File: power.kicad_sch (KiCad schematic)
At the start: 6 parts, among them U6 REF3030, U7 MIC920YC5-TR

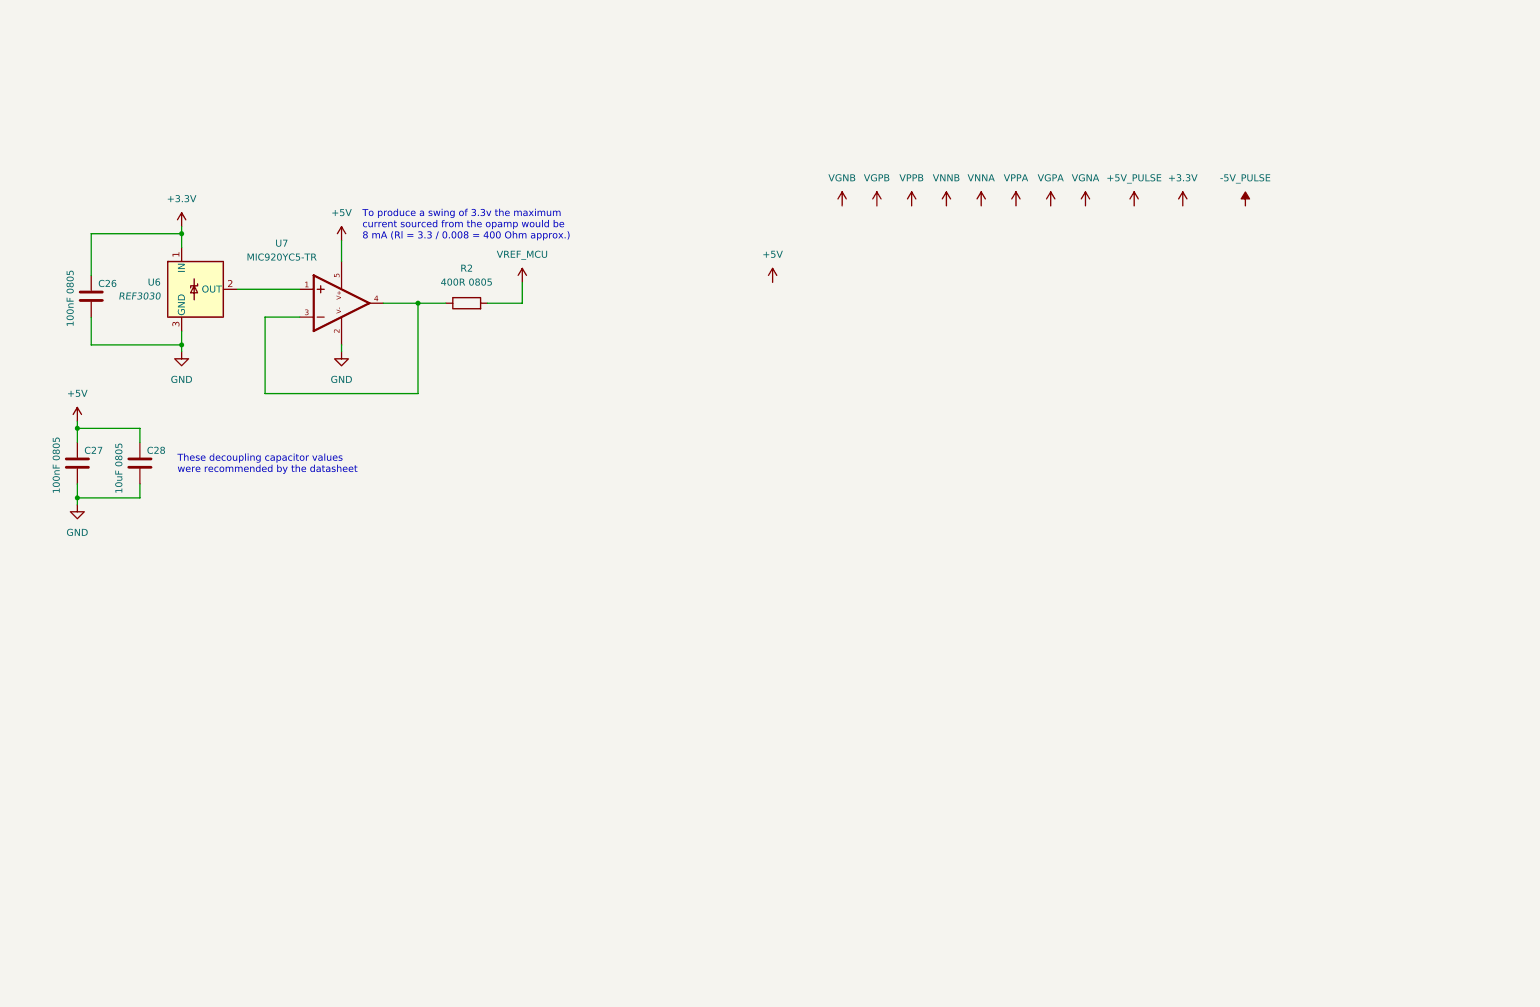
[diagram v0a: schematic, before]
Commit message: finished analog signal chain, added main power components, complete the schematic and form a power budget table
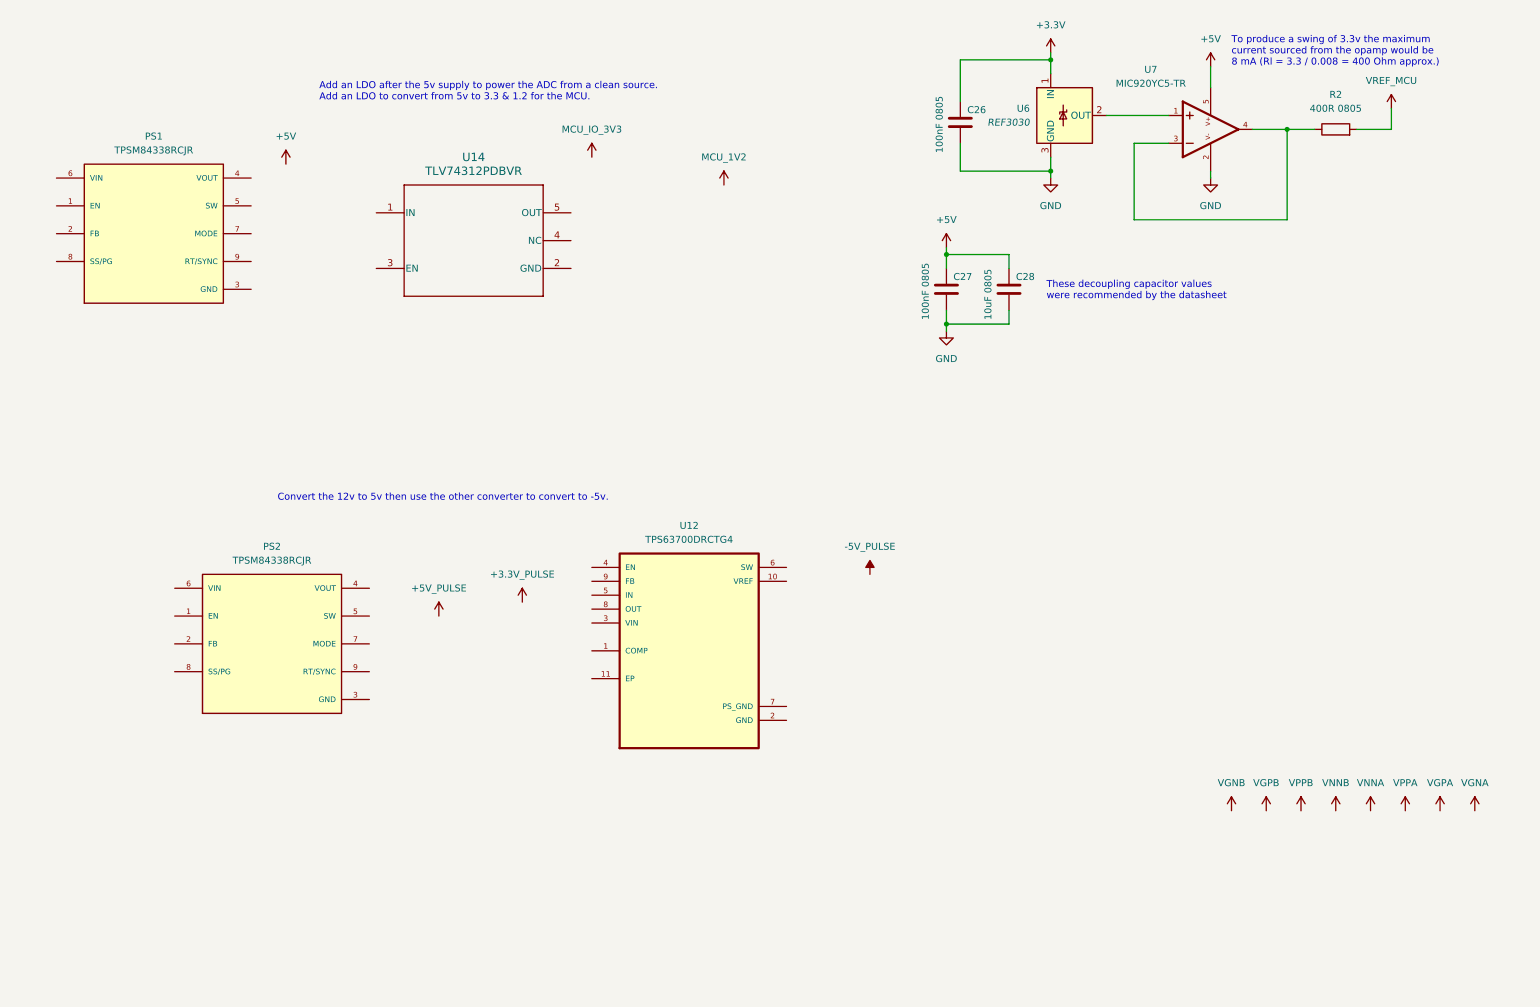
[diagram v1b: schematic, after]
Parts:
- added PS1, PS2: TPSM84338RCJR, TPSM84338RCJR:CONV_TPSM84338RCJR, symbol TPSM84338RCJR:TPSM84338RCJR
- added U12: TPS63700DRCTG4, TPS63700DRCTG4:VREG_V62_16624-01YE, symbol TPS63700DRCTG4:TPS63700DRCTG4
- added U14: TLV74312PDBVR, DBV0005A_N, symbol TLV74312PDBVR:TLV74312PDBVR
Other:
- note added: "Add an LDO after the 5v supply to power the ADC from a clean source. Add an LDO to convert from 5v to 3.3 & 1.2 for the MCU."
- note added: "Convert the 12v to 5v then use the other converter to convert to -5v."
- moved on the sheet: C26, C27, C28, R2, U6, U7

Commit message: finished 50% of power section, 50% remaining + EEPROM & revision
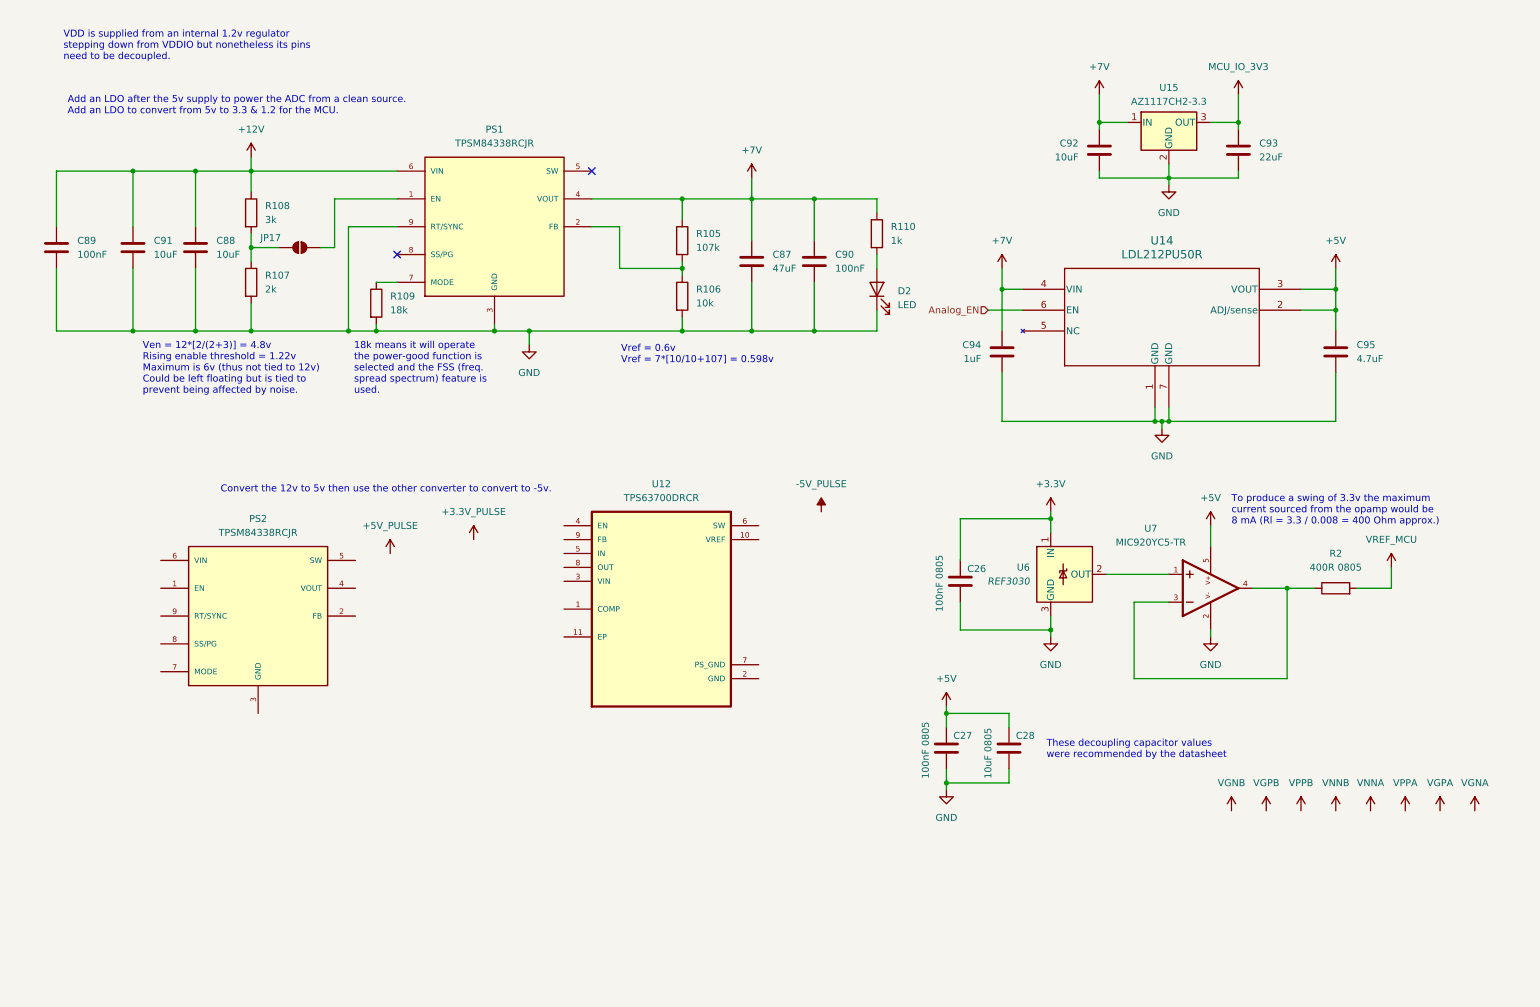
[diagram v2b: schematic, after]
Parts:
- removed U12: TPS63700DRCTG4, TPS63700DRCTG4:VREG_V62_16624-01YE, symbol TPS63700DRCTG4:TPS63700DRCTG4
- removed U14: TLV74312PDBVR, DBV0005A_N, symbol TLV74312PDBVR:TLV74312PDBVR
- added C87: 47uF, symbol Device:C
- added C88, C91, C92: 10uF, symbol Device:C
- added C89, C90: 100nF, symbol Device:C
- added C93: 22uF, symbol Device:C
- added C94: 1uF, symbol Device:C
- added C95: 4.7uF, symbol Device:C
- added D2: LED, symbol Device:LED
- added JP17: SolderJumper_2_Open, symbol Jumper:SolderJumper_2_Open
- added R105: 107k, symbol Device:R
- added R106: 10k, symbol Device:R
- added R107: 2k, symbol Device:R
- added R108: 3k, symbol Device:R
- added R109: 18k, symbol Device:R
- added R110: 1k, symbol Device:R
- added U12: TPS63700DRCR, TPS63700DRCR:VREG_V62_16624-01YE, symbol TPS63700DRCR:TPS63700DRCR
- added U14: LDL212PU50R, DFN_2PU50R_STM, symbol 2025-12-15_21-20-32:LDL212PU50R
- added U15: AZ1117CH2-3.3, Package_TO_SOT_SMD:SOT-223-3_TabPin2, symbol Regulator_Linear:AZ1117CH2-3.3
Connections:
- net +5V: now also C95.1, U14.2 (ADJ/sense), U14.3 (VOUT)
- net GND: now also PS1.3 (GND), PS1.9 (RT/SYNC), C87.2, C88.2, C89.2, C90.2, C91.2, C92.2, C93.2, C94.2, C95.2, D2.1 (K), R106.2, R107.2, R109.2, U14.1 (GND), U14.7 (GND), U15.2 (GND)
- net MCU_IO_3V3: now also C93.1, U15.3 (OUT)
- net at PS1.1 (EN): now also JP17.2 (B)
- net at PS1.2 (FB): now also R105.2, R106.1
- net +7V: now reaches PS1.4 (VOUT)
- net +7V: now also C87.1, C90.1, C92.1, C94.1, R105.1, R110.1, U14.4 (VIN), U15.1 (IN)
- net +12V: now reaches PS1.6 (VIN)
- net +12V: now also C88.1, C89.1, C91.1, R108.1
- net at PS1.7 (MODE): now also R109.1
- new net: JP17.1 (A), R107.1, R108.2
- new net: D2.2 (A), R110.2
- new net Analog_EN: U14.6 (EN)
- no-connect marks 0 -> 2
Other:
- note added: "18k means it will operate the power-good function is selected and the FSS (freq. spread spectrum) feature is used."
- note added: "VDD is supplied from an internal 1.2v regulator stepping down from VDDIO but nonetheless its pins need to be decoupled."
- note added: "Ven = 12*[2/(2+3)] = 4.8v Rising enable threshold = 1.22v Maximum is 6v (thus not tied to 12v) Could be left floating but is tied to prevent being affected by noise."
- note added: "Vref = 0.6v Vref = 7*[10/10+107] = 0.598v"
- moved on the sheet: C26, C27, C28, PS1, R2, U6, U7

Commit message: 95% done, only headers for communication & power are remaining + RS232 transceiver & 1.5v reference
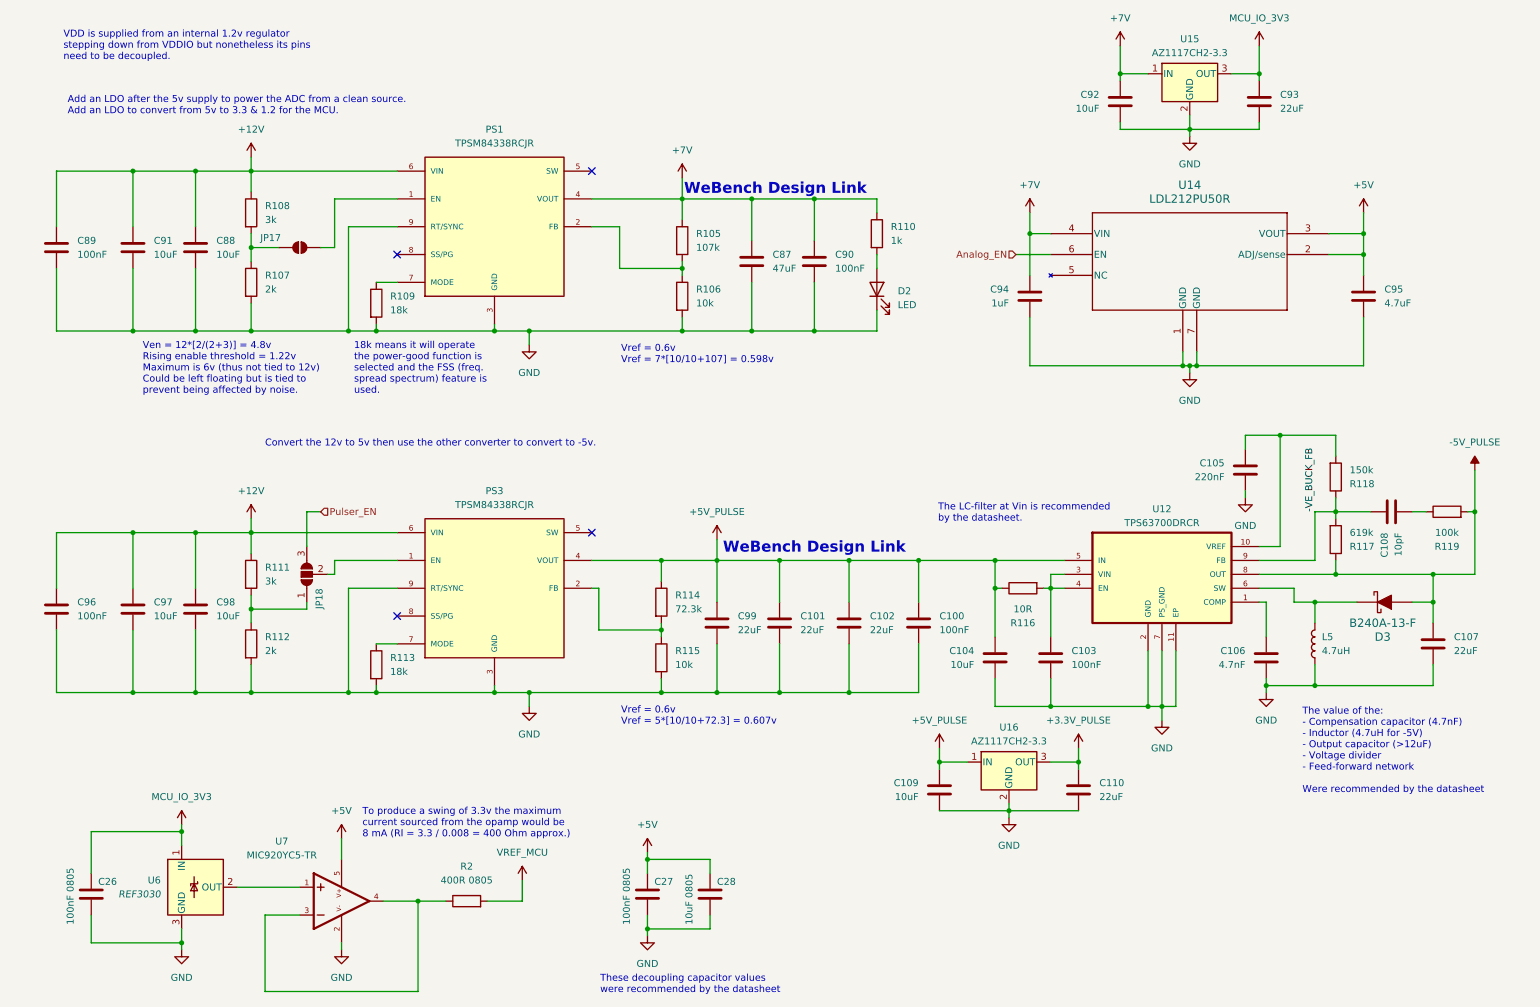
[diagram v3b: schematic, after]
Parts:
- removed PS2: TPSM84338RCJR, TPSM84338RCJR:CONV_TPSM84338RCJR, symbol TPSM84338RCJR:TPSM84338RCJR
- added C100, C103, C96: 100nF, symbol Device:C
- added C101, C102, C107, C110, C99: 22uF, symbol Device:C
- added C104, C109, C97, C98: 10uF, symbol Device:C
- added C105: 220nF, symbol Device:C
- added C106: 4.7nF, symbol Device:C
- added C108: 10pF, symbol Device:C
- added D3: B240A-13-F, digikey-footprints:DO-214AC, symbol dk_Diodes-Rectifiers-Single:B240A-13-F
- added JP18: SolderJumper_3_Open, symbol Jumper:SolderJumper_3_Open
- added L5: 4.7uH, symbol Device:L
- added PS3: TPSM84338RCJR, TPSM84338RCJR:CONV_TPSM84338RCJR, symbol TPSM84338RCJR:TPSM84338RCJR
- added R111: 3k, symbol Device:R
- added R112: 2k, symbol Device:R
- added R113: 18k, symbol Device:R
- added R114: 72.3k, symbol Device:R
- added R115: 10k, symbol Device:R
- added R116: 10R, symbol Device:R
- added R117: 619k, symbol Device:R
- added R118: 150k, symbol Device:R
- added R119: 100k, symbol Device:R
- added U16: AZ1117CH2-3.3, Package_TO_SOT_SMD:SOT-223-3_TabPin2, symbol Regulator_Linear:AZ1117CH2-3.3
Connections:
- net +3.3V is gone; now on net MCU_IO_3V3: C26.1, U6.1 (IN)
- net +12V: now also C96.1, C97.1, C98.1, PS3.6 (VIN), R111.1
- net +3.3V_PULSE: now also C110.1, U16.3 (OUT)
- net +5V_PULSE: now also U12.5 (IN), C100.1, C101.1, C102.1, C104.1, C109.1, C99.1, PS3.4 (VOUT), R114.1, R116.1, U16.1 (IN)
- net -5V_PULSE: now also U12.8 (OUT), C107.1, D3.A, R117.1, R119.2
- net GND: now also U12.11 (EP), U12.2 (GND), U12.7 (PS_GND), C100.2, C101.2, C102.2, C103.2, C104.2, C105.2, C106.2, C107.2, C109.2, C110.2, C96.2, C97.2, C98.2, C99.2, L5.1, PS3.3 (GND), PS3.9 (RT/SYNC), R112.2, R113.2, R115.2, U16.2 (GND)
- net at U12.1 (COMP): now also C106.1
- net at U12.10 (VREF): now also C105.1, R118.2
- net at U12.3 (VIN): now also U12.4 (EN), C103.1, R116.2
- net at U12.6 (SW): now also D3.K, L5.2
- net -VE_BUCK_FB: now reaches U12.9 (FB)
- net -VE_BUCK_FB: now also C108.1, R117.2, R118.1
- new net: JP18.1 (A), R111.2, R112.1
- new net: PS3.2 (FB), R114.2, R115.1
- new net: JP18.2 (C), PS3.1 (EN)
- new net: PS3.7 (MODE), R113.1
- new net: C108.2, R119.1
- new net Pulser_EN: JP18.3 (B)
- no-connect marks 2 -> 4
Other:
- note added: "The LC-filter at Vin is recommended by the datasheet."
- note added: "The value of the: - Compensation capacitor (4.7nF) - Inductor (4.7uH for -5V) - Output capacitor (>12uF) - Voltage divider - Feed-forward network Were recommended by the datasheet"
- note added: "Vref = 0.6v Vref = 5*[10/10+72.3] = 0.607v"
- note added: "WeBench Design Link"
- moved on the sheet: C26, C27, C28, C92, C93, C94, C95, R2, U12, U14, U15, U6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

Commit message: DONE (inshallah)
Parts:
- added D4, D5, D6, D7, D8: LED, symbol Device:LED
- added J17: Input Power, symbol Connector:Screw_Terminal_01x02
- added R136, R137: 1k, symbol Device:R
- added R138: 2k, symbol Device:R
- added R139, R140: 330R, symbol Device:R
- added TP73, TP74, TP75, TP76, TP77, TP78, TP79, TP80, TP81: RCT-0C, digikey-footprints:PROBE_PAD_0805, symbol dk_Test-Points:RCT-0C
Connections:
- net +12V: now also J17.1 (Pin_1), R138.1, TP73.1
- net +3.3V_PULSE: now also R140.1, TP78.1
- net +5V: now also R137.1, TP77.1
- net +5V_PULSE: now also R136.1, TP75.1
- net +7V: now also TP74.1
- net -5V_PULSE: now also TP76.1
- net GND: now also D4.1 (K), D5.1 (K), D6.1 (K), D7.1 (K), D8.1 (K), J17.2 (Pin_2)
- net MCU_IO_3V3: now also R139.1, TP79.1
- net VREF_MCU: now also TP80.1
- net at U6.2 (OUT), U7.1: now also TP81.1
- new net: D6.2 (A), R138.2
- new net: D8.2 (A), R140.2
- new net: D7.2 (A), R139.2
- new net: D4.2 (A), R136.2
- new net: D5.2 (A), R137.2
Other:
- note added: "The values of the: - Compensation capacitor (4.7nF) - Inductor (4.7uH for -5V) - Output capacitor (>12uF) - Voltage divider - Feed-forward network Were recommended by the datasheet"
- note removed: "Add an LDO after the 5v supply to power the ADC from a clean source. Add an LDO to convert from 5v to 3.3 & 1.2 for the MCU."
- note removed: "The value of the: - Compensation capacitor (4.7nF) - Inductor (4.7uH for -5V) - Output capacitor (>12uF) - Voltage divider - Feed-forward network Were recommended by the datasheet"

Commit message: started layout, 20-30% done
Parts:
- added J26: Spectrography Power, Connector_PinHeader_2.54mm:PinHeader_1x02_P2.54mm_Vertical, symbol Connector:Conn_01x02_Pin
- C100, C103, C105, C106, C108, C26, C27, C28, C89, C90, C94, C96: footprint (none) -> Capacitor_SMD:C_0603_1608Metric
- C101, C102, C104, C107, C109, C110, C88, C91, C92, C93, C95, C97, C98, C99: footprint (none) -> Capacitor_SMD:C_0805_2012Metric
- C87: footprint (none) -> Capacitor_SMD:C_1210_3225Metric
- D2, D4, D5, D6, D7, D8: footprint (none) -> LED_SMD:LED_0805_2012Metric
- J17: footprint (none) -> TerminalBlock:TerminalBlock_MaiXu_MX126-5.0-02P_1x02_P5.00mm
- JP17: footprint (none) -> Jumper:SolderJumper-2_P1.3mm_Open_Pad1.0x1.5mm
- JP18: footprint (none) -> Jumper:SolderJumper-3_P1.3mm_Open_Pad1.0x1.5mm
- L5: footprint (none) -> Inductor_SMD:L_0805_2012Metric
- R105, R106, R107, R108, R109, R110, R111, R112, R113, R114, R115, R116, R117, R118, R119, R136, R137, R138, R139, R140, R2: footprint (none) -> Resistor_SMD:R_0603_1608Metric
- U14: footprint DFN_2PU50R_STM -> LDL212PU50R:DFN_2PU50R_STM
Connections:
- net +12V: now also J26.1 (Pin_1)
- net GND: now also J26.2 (Pin_2)
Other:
- note removed: "Convert the 12v to 5v then use the other converter to convert to -5v."

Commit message: 5% left, rearrange ADC channels for right AFE
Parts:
- added JP10, JP13, JP6, JP8, JP9: SolderJumper_2_Open, Jumper:SolderJumper-2_P1.3mm_Open_RoundedPad1.0x1.5mm, symbol Jumper:SolderJumper_2_Open
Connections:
- net +12V: now also JP6.1 (A), JP8.1 (A); no longer C88.1, C89.1, C91.1, C96.1, C97.1, C98.1, PS1.6 (VIN), PS3.6 (VIN), R108.1, R111.1, TP73.1
- net +5V: now also JP13.1 (A); no longer C27.1, C28.1, U7.5
- net +7V: now also JP9.1 (A); no longer C92.1, C94.1, U14.4 (VIN), U15.1 (IN)
- net MCU_IO_3V3: now also JP10.2 (B); no longer C93.1, R139.1, TP79.1, U15.3 (OUT)
- new net +12V_VFD: C88.1, C89.1, C91.1, C96.1, C97.1, C98.1, JP6.2 (B), JP8.2 (B), PS1.6 (VIN), PS3.6 (VIN), R108.1, R111.1, TP73.1
- new net +3.3V: C93.1, JP10.1 (A), R139.1, TP79.1, U15.3 (OUT)
- new net +5V_VFD: C27.1, C28.1, JP13.2 (B), U7.5
- new net +7V_VFD: C92.1, C94.1, JP9.2 (B), U14.4 (VIN), U15.1 (IN)
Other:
- moved on the sheet: J26, TP74

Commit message: added test points & fuse
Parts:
- removed TP80, TP81: RCT-0C, digikey-footprints:PROBE_PAD_0805, symbol dk_Test-Points:RCT-0C
- added F1: 0154001.DR, 0154001.DR:FUSE_0154001.DR, symbol 0154001.DR:0154001.DR
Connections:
- net +12V: now also JP8.2 (B), F1.2; no longer J17.1 (Pin_1), JP8.1 (A)
- net +12V_VFD: now also JP8.1 (A); no longer JP8.2 (B)
- new net: F1.1, J17.1 (Pin_1)
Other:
- moved on the sheet: D6, J17, JP18, JP8, R138
